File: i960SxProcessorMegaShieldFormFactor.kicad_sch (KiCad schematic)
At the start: 35 parts, among them P1 Power, P2 Data Lines Lower, P3 Data Lines Upper, P4 Address Lines, P5 PWM, P6 Serializable Pins, P7 1284p Direct Connection, U1 74HC245, U2 74HC245, U3 80960Sx

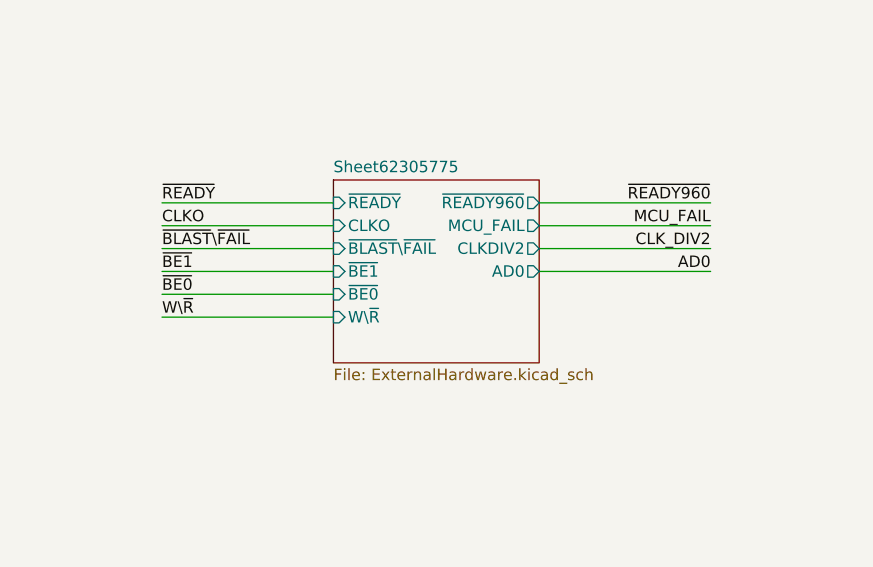
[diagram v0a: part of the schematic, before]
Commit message: Use PLCC20 for the GAL chip instead of the much larger DIP20
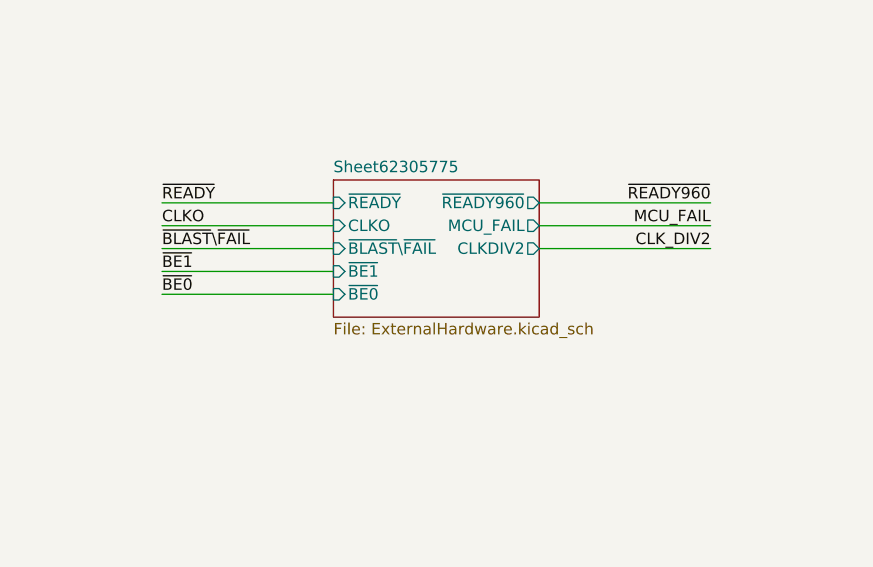
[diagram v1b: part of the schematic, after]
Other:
- sheet Sheet62305775 ports: added none; removed AD0, W\~{R}
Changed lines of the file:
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@@
-    (stroke (width 0) (type default) (color 0 0 0 0))
-  )
-  (wire (pts (xy 323.85 205.74) (xy 342.9 205.74))
     (stroke (width 0) (type default) (color 0 0 0 0))
   )
@@
   )
   (wire (pts (xy 93.98 90.17) (xy 63.5 90.17))
-    (stroke (width 0) (type default) (color 0 0 0 0))
-  )
-  (wire (pts (xy 365.76 200.66) (xy 384.81 200.66))
     (stroke (width 0) (type default) (color 0 0 0 0))
   )
@@
   )
   (label "A18" (at 63.5 77.47 180)
-    (effects (font (size 1.27 1.27)) (justify right bottom))
-  )
-  (label "W\\~{R}" (at 323.85 205.74 0)
-    (effects (font (size 1.27 1.27)) (justify left bottom))
-  )
-  (label "AD0" (at 384.81 200.66 180)
     (effects (font (size 1.27 1.27)) (justify right bottom))
   )
@@
     (pin "1")
   )
-  (sheet (at 342.9 190.5) (size 22.86 20.32) (fields_autoplaced)
+  (sheet (at 342.9 190.5) (size 22.86 15.24) (fields_autoplaced)
     (stroke (width 0) (type solid) (color 0 0 0 0))
     (fill (color 0 0 0 0.0000))
@@
       (effects (font (size 1.27 1.27)) (justify left bottom))
     )
-    (property "Sheet file" "ExternalHardware.kicad_sch" (id 1) (at 342.9 211.4046 0)
+    (property "Sheet file" "ExternalHardware.kicad_sch" (id 1) (at 342.9 206.3246 0)
       (effects (font (size 1.27 1.27)) (justify left top))
     )
@@
     )
     (pin "CLKDIV2" output (at 365.76 198.12 0)
-      (effects (font (size 1.27 1.27)) (justify right))
-    )
-    (pin "W\\~{R}" input (at 342.9 205.74 180)
-      (effects (font (size 1.27 1.27)) (justify left))
-    )
-    (pin "AD0" output (at 365.76 200.66 0)
       (effects (font (size 1.27 1.27)) (justify right))
     )
@@
       (reference "#PWR019") (unit 1) (value "GND") (footprint "")
     )
-    (path "/00000000-0000-0000-0000-000062305776/c87d717f-47b5-4cbc-92c9-1f27489443fc"
-      (reference "#PWR020") (unit 1) (value "+5V") (footprint "")
-    )
-    (path "/00000000-0000-0000-0000-000062305776/99f40a50-ee35-472a-8a7f-9dca1993ec33"
-      (reference "#PWR021") (unit 1) (value "GND") (footprint "")
-    )
     (path "/00000000-0000-0000-0000-000056d758f6"
       (reference "#PWR022") (unit 1) (value "GND") (footprint "")
@@
       (reference "C17") (unit 1) (value "0.1uF") (footprint "Capacitor_SMD:C_0805_2012Metric_Pad1.18x1.45mm_HandSolder")
     )
-    (path "/00000000-0000-0000-0000-000062305776/68b9a284-29e4-4461-9b3a-9f4ef09e2dc9"
-      (reference "C18") (unit 1) (value "0.1uF") (footprint "Capacitor_THT:C_Disc_D5.0mm_W2.5mm_P2.50mm")
-    )
     (path "/00000000-0000-0000-0000-000062305776/37cf12d2-9997-4855-9d67-d21913190832"
       (reference "C19") (unit 1) (value "0.1uF") (footprint "Capacitor_THT:C_Disc_D5.0mm_W2.5mm_P2.50mm")
@@
       (reference "U3") (unit 1) (value "80960Sx") (footprint "Package_LCC:PLCC-84_THT-Socket")
     )
-    (path "/00000000-0000-0000-0000-000062305776/9fb0fc0c-649f-4b6a-8681-4c1c3cff265d"
-      (reference "U6") (unit 1) (value "74AHC74") (footprint "Package_SO:SOIC-14_3.9x8.7mm_P1.27mm")
-    )
-    (path "/00000000-0000-0000-0000-000062305776/05566c90-9ff9-4de8-a5f1-1d8176493d23"
-      (reference "U6") (unit 2) (value "74AHC74") (footprint "Package_SO:SOIC-14_3.9x8.7mm_P1.27mm")
-    )
-    (path "/00000000-0000-0000-0000-000062305776/da30d552-383a-40ee-b502-3261b6b0380f"
-      (reference "U6") (unit 3) (value "74AHC74") (footprint "Package_SO:SOIC-14_3.9x8.7mm_P1.27mm")
-    )
     (path "/00000000-0000-0000-0000-000062305776/67f3f848-2b47-48d4-8ef6-b211a1c5ad8a"
       (reference "U7") (unit 1) (value "74AHC74") (footprint "Package_SO:SOIC-14_3.9x8.7mm_P1.27mm")
@@
     )
     (path "/00000000-0000-0000-0000-000062305776/312ed157-03e4-4f79-8162-ee244f6128f1"
-      (reference "U8") (unit 1) (value "GAL16V8") (footprint "Package_DIP:DIP-20_W7.62mm_Socket")
+      (reference "U8") (unit 1) (value "GAL16V8") (footprint "Package_LCC:PLCC-20_THT-Socket")
     )
     (path "/c11f357c-f8ce-40dd-a2b5-d959d6b2f47e"

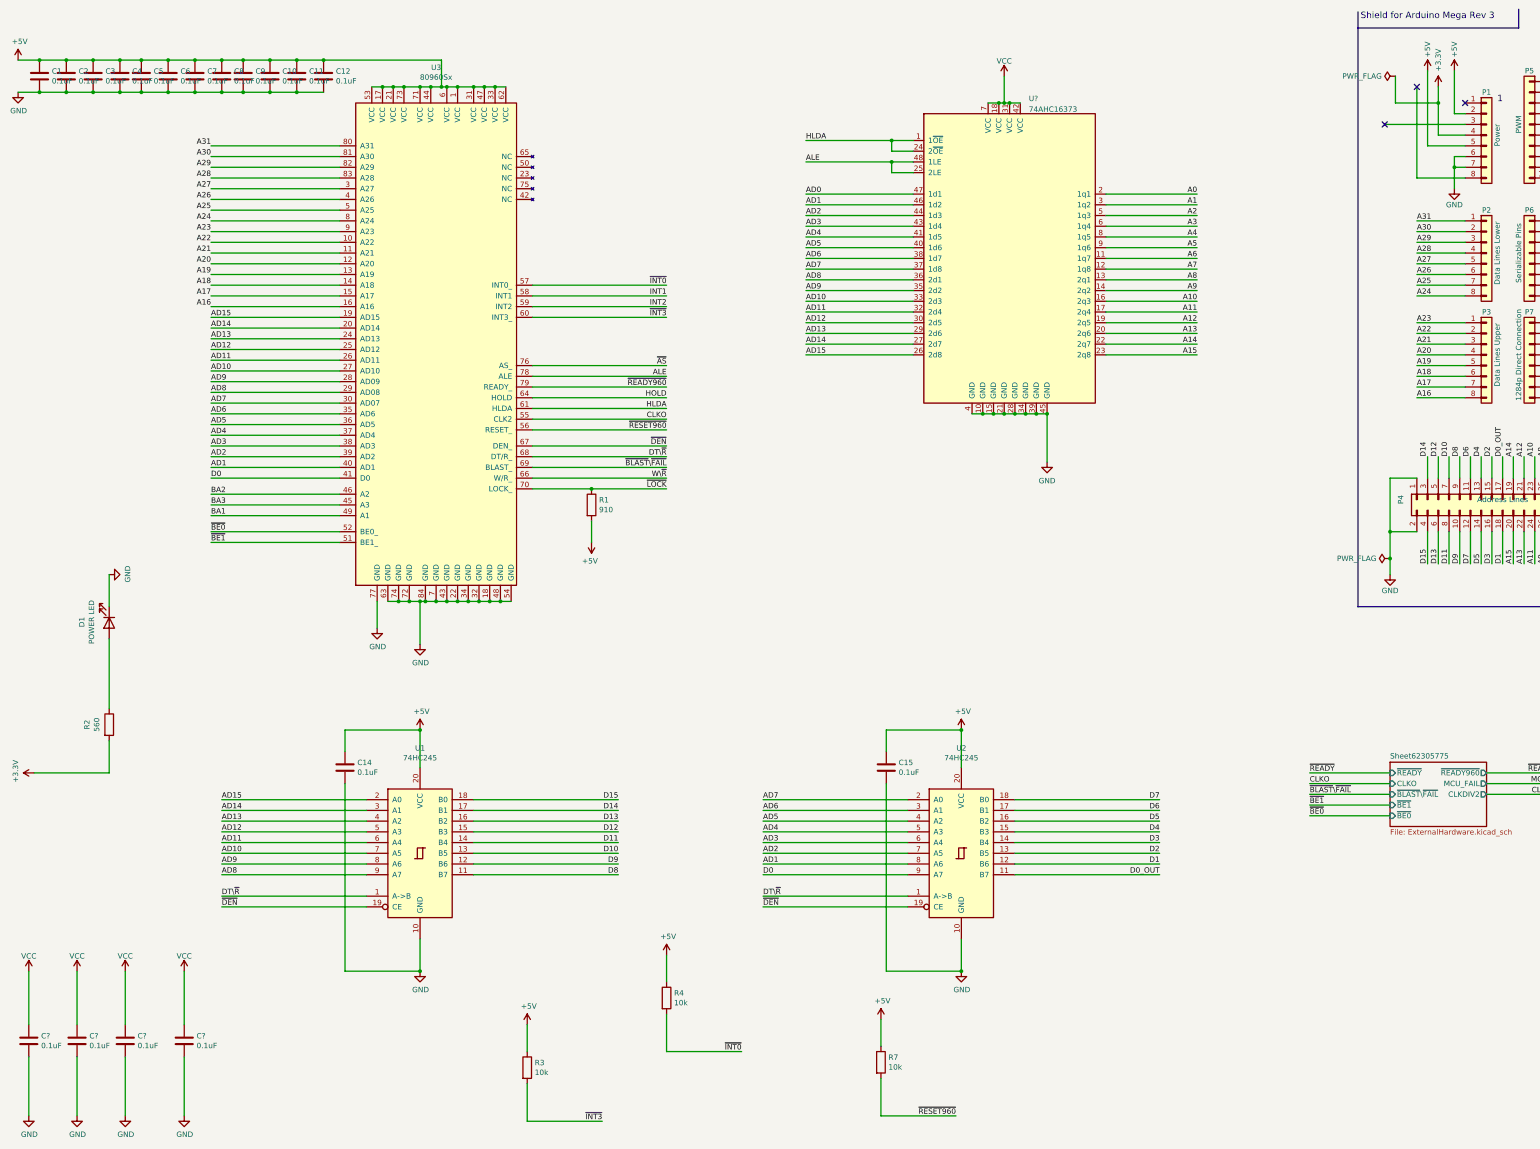
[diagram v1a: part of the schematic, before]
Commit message: Introduce the 74LVC16T245 for the datalines
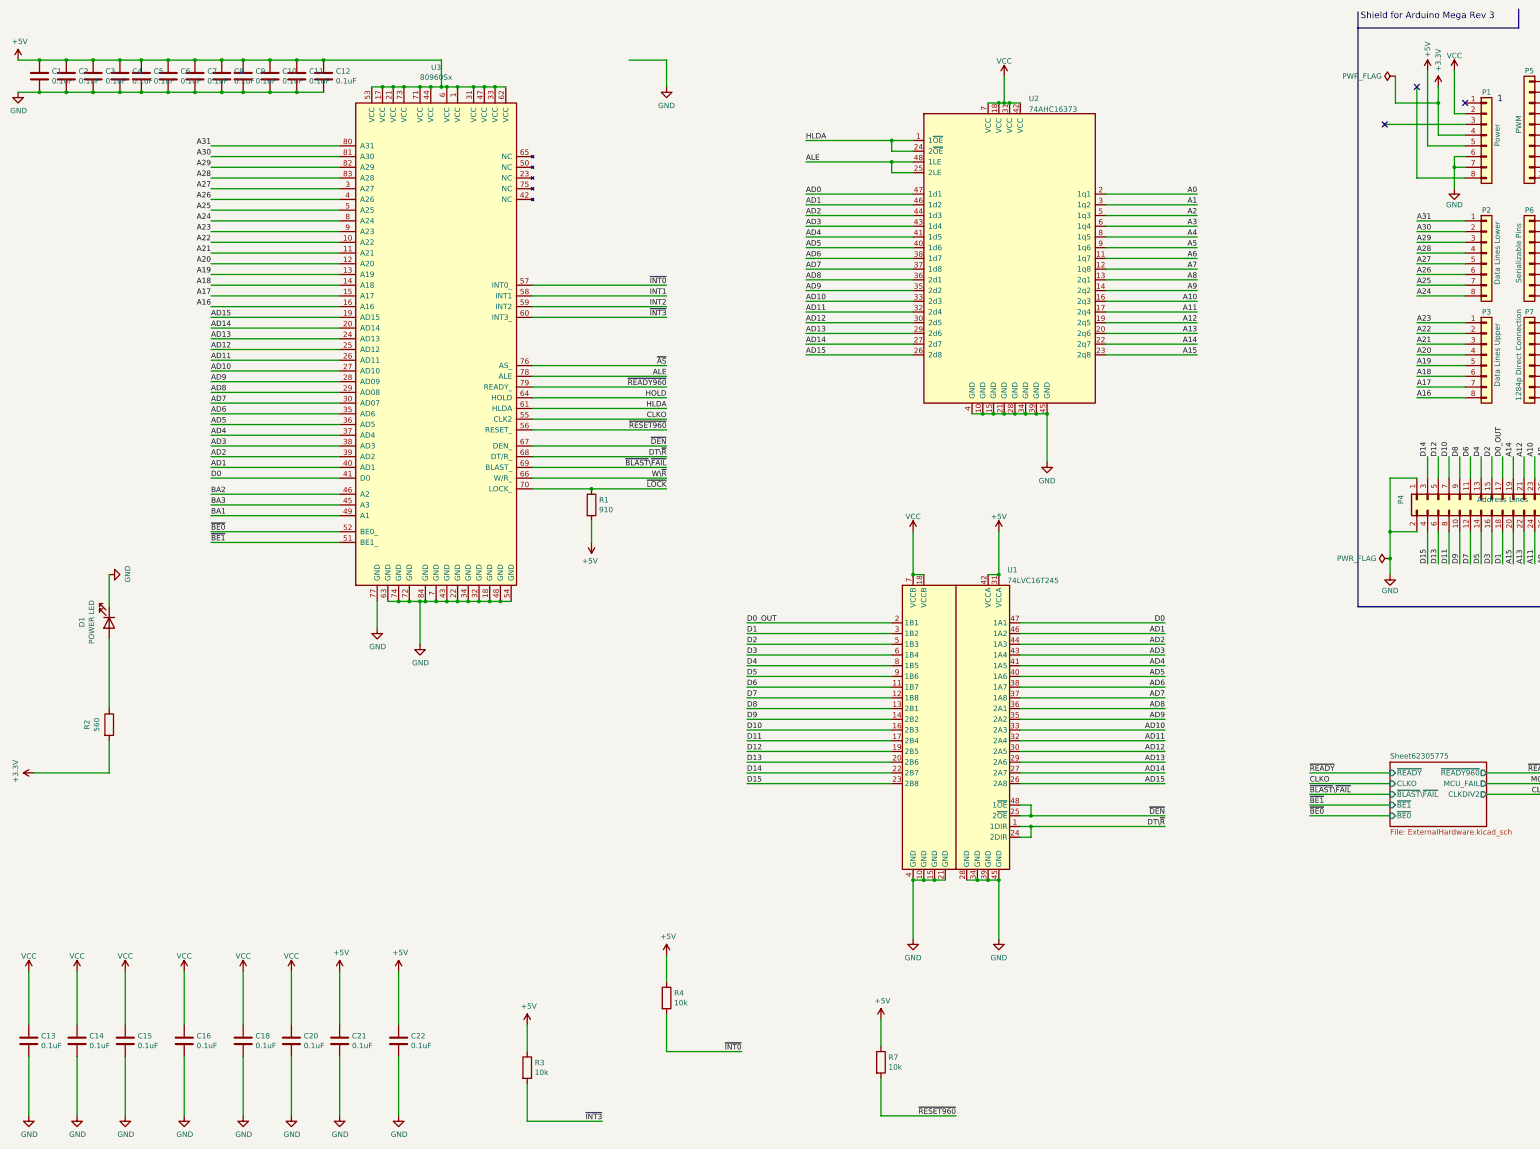
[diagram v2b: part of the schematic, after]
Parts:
- removed C14, C15: 0.1uF, Capacitor_SMD:C_0805_2012Metric_Pad1.18x1.45mm_HandSolder, symbol Device:C
- removed U1, U2: 74HC245, Package_SO:SOIC-20W_7.5x12.8mm_P1.27mm, symbol 74xx:74HC245
- added C18, C20, C21, C22: 0.1uF, Capacitor_SMD:C_0805_2012Metric_Pad1.18x1.45mm_HandSolder, symbol Device:C
- added U1: 74LVC16T245, Package_SO:TSSOP-48_6.1x12.5mm_P0.5mm, symbol LogicLevelTranslators:74LVC16T245
- gave numbers to parts that had none: 5
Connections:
- net +5V: now also C21.1, C22.1, U1.31 (VCCA), U1.42 (VCCA); no longer P1.2 (Pin_2)
- net AD1: now also U1.46 (1A2)
- net AD10: now also U1.33 (2A3)
- net AD11: now also U1.32 (2A4)
- net AD12: now also U1.30 (2A5)
- net AD13: now also U1.29 (2A6)
- net AD14: now also U1.27 (2A7)
- net AD15: now also U1.26 (2A8)
- net AD2: now also U1.44 (1A3)
- net AD3: now also U1.43 (1A4)
- net AD4: now also U1.41 (1A5)
- net AD5: now also U1.40 (1A6)
- net AD6: now also U1.38 (1A7)
- net AD7: now also U1.37 (1A8)
- net AD8: now also U1.36 (2A1)
- net AD9: now also U1.35 (2A2)
- net D0: now also U1.47 (1A1)
- net D0_OUT: now also U1.2 (1B1)
- net D1: now also U1.3 (1B2)
- net D10: now also U1.16 (2B3)
- net D11: now also U1.17 (2B4)
- net D12: now also U1.19 (2B5)
- net D13: now also U1.20 (2B6)
- net D14: now also U1.22 (2B7)
- net D15: now also U1.23 (2B8)
- net D2: now also U1.5 (1B3)
- net D3: now also U1.6 (1B4)
- net D4: now also U1.8 (1B5)
- net D5: now also U1.9 (1B6)
- net D6: now also U1.11 (1B7)
- net D7: now also U1.12 (1B8)
- net D8: now also U1.13 (2B1)
- net D9: now also U1.14 (2B2)
- net DT\~{R}: now also U1.1 (1DIR), U1.24 (2DIR)
- net GND: now also C18.2, C20.2, C21.2, C22.2, U1.10 (GND), U1.15 (GND), U1.21 (GND), U1.28 (GND), U1.34 (GND), U1.39 (GND), U1.4 (GND), U1.45 (GND)
- net VCC: now also P1.2 (Pin_2), C18.1, C20.1, U1.18 (VCCB), U1.7 (VCCB)
- net ~{DEN}: now also U1.25 (2~{OE}), U1.48 (1~{OE})

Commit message: Just do the consolidation
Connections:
- net A0: now also U2.23 (2q8); no longer U2.2 (1q1)
- net A1: now also U2.22 (2q7); no longer U2.3 (1q2)
- net A10: now also U2.9 (1q6); no longer U2.16 (2q3)
- net A11: now also U2.8 (1q5); no longer U2.17 (2q4)
- net A12: now also U2.6 (1q4); no longer U2.19 (2q5)
- net A13: now also U2.5 (1q3); no longer U2.20 (2q6)
- net A14: now also U2.3 (1q2); no longer U2.22 (2q7)
- net A15: now also U2.2 (1q1); no longer U2.23 (2q8)
- net A2: now also U2.20 (2q6); no longer U2.5 (1q3)
- net A3: now also U2.19 (2q5); no longer U2.6 (1q4)
- net A4: now also U2.17 (2q4); no longer U2.8 (1q5)
- net A5: now also U2.16 (2q3); no longer U2.9 (1q6)
- net A6: now also U2.14 (2q2); no longer U2.11 (1q7)
- net A7: now also U2.13 (2q1); no longer U2.12 (1q8)
- net A8: now also U2.12 (1q8); no longer U2.13 (2q1)
- net A9: now also U2.11 (1q7); no longer U2.14 (2q2)
- net AD0: now also U2.26 (2d8); no longer U2.47 (1d1)
- net AD1: now also U1.27 (2A7), U2.27 (2d7); no longer U1.46 (1A2), U2.46 (1d2)
- net AD10: now also U1.40 (1A6), U2.40 (1d6); no longer U1.33 (2A3), U2.33 (2d3)
- net AD11: now also U1.41 (1A5), U2.41 (1d5); no longer U1.32 (2A4), U2.32 (2d4)
- net AD12: now also U1.43 (1A4), U2.43 (1d4); no longer U1.30 (2A5), U2.30 (2d5)
- net AD13: now also U1.44 (1A3), U2.44 (1d3); no longer U1.29 (2A6), U2.29 (2d6)
- net AD14: now also U1.46 (1A2), U2.46 (1d2); no longer U1.27 (2A7), U2.27 (2d7)
- net AD15: now also U1.47 (1A1), U2.47 (1d1); no longer U1.26 (2A8), U2.26 (2d8)
- net AD2: now also U1.29 (2A6), U2.29 (2d6); no longer U1.44 (1A3), U2.44 (1d3)
- net AD3: now also U1.30 (2A5), U2.30 (2d5); no longer U1.43 (1A4), U2.43 (1d4)
- net AD4: now also U1.32 (2A4), U2.32 (2d4); no longer U1.41 (1A5), U2.41 (1d5)
- net AD5: now also U1.33 (2A3), U2.33 (2d3); no longer U1.40 (1A6), U2.40 (1d6)
- net AD6: now also U1.35 (2A2), U2.35 (2d2); no longer U1.38 (1A7), U2.38 (1d7)
- net AD7: now also U1.36 (2A1), U2.36 (2d1); no longer U1.37 (1A8), U2.37 (1d8)
- net AD8: now also U1.37 (1A8), U2.37 (1d8); no longer U1.36 (2A1), U2.36 (2d1)
- net AD9: now also U1.38 (1A7), U2.38 (1d7); no longer U1.35 (2A2), U2.35 (2d2)
- net D0: now also U1.26 (2A8); no longer U1.47 (1A1)
- net D0_OUT: now also U1.23 (2B8); no longer U1.2 (1B1)
- net D1: now also U1.22 (2B7); no longer U1.3 (1B2)
- net D10: now also U1.9 (1B6); no longer U1.16 (2B3)
- net D11: now also U1.8 (1B5); no longer U1.17 (2B4)
- net D12: now also U1.6 (1B4); no longer U1.19 (2B5)
- net D13: now also U1.5 (1B3); no longer U1.20 (2B6)
- net D14: now also U1.3 (1B2); no longer U1.22 (2B7)
- net D15: now also U1.2 (1B1); no longer U1.23 (2B8)
- net D2: now also U1.20 (2B6); no longer U1.5 (1B3)
- net D3: now also U1.19 (2B5); no longer U1.6 (1B4)
- net D4: now also U1.17 (2B4); no longer U1.8 (1B5)
- net D5: now also U1.16 (2B3); no longer U1.9 (1B6)
- net D6: now also U1.14 (2B2); no longer U1.11 (1B7)
- net D7: now also U1.13 (2B1); no longer U1.12 (1B8)
- net D8: now also U1.12 (1B8); no longer U1.13 (2B1)
- net D9: now also U1.11 (1B7); no longer U1.14 (2B2)

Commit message: Finished retracing
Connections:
- net AD0 is gone; now on net GND: U2.26 (2d8)
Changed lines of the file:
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@@
+    (effects (font (size 1.27 1.27)) (justify left bottom))
+  )
+  (label "AD0" (at 162.56 24.13 0)
     (effects (font (size 1.27 1.27)) (justify left bottom))
   )

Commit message: Remove a resistor and drop the 10MHz output clock
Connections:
- net CLK_DIV2: no longer P5.1 (Pin_1)
- net ~{READY}: no longer P5.6 (Pin_6)
- no-connect marks 4 -> 6
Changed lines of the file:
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@@
   (no_connect (at 349.25 30.48))
   (no_connect (at 398.78 39.37))
+  (no_connect (at 398.78 41.91))
   (no_connect (at 341.63 39.37))
   (no_connect (at 360.68 34.29))
+  (no_connect (at 398.78 29.21))
   (wire (pts (xy 381 46.99) (xy 398.78 46.99))
     (stroke (width 0) (type default) (color 0 0 0 0))
@@
     (effects (font (size 1.27 1.27)) (justify left bottom))
   )
-  (label "~{READY}" (at 398.78 41.91 180)
-    (effects (font (size 1.27 1.27)) (justify right bottom))
-  )
   (label "~{INT3}" (at 156.21 275.59 180)
     (effects (font (size 1.27 1.27)) (justify right bottom))
@@
     (effects (font (size 1.27 1.27)) (justify right bottom))
   )
-  (label "CLK_DIV2" (at 398.78 29.21 180)
-    (effects (font (size 1.27 1.27)) (justify right bottom))
-  )
   (label "AD9" (at 63.5 100.33 0)
     (effects (font (size 1.27 1.27)) (justify left bottom))
@@
       (reference "#PWR026") (unit 1) (value "GND") (footprint "")
     )
-    (path "/00000000-0000-0000-0000-000062305776/7e6268bd-de28-4e45-b872-c2d5289de35e"
-      (reference "#PWR027") (unit 1) (value "+5V") (footprint "")
-    )
     (path "/00000000-0000-0000-0000-000062305776/0e2482b9-a689-45a3-a536-674e09a602a2"
       (reference "#PWR028") (unit 1) (value "+5V") (footprint "")
@@
       (reference "R4") (unit 1) (value "10k") (footprint "Resistor_SMD:R_0805_2012Metric_Pad1.20x1.40mm_HandSolder")
     )
-    (path "/00000000-0000-0000-0000-000062305776/c5053a4e-ffe0-455f-8838-52320f5821ec"
-      (reference "R5") (unit 1) (value "10k") (footprint "Resistor_SMD:R_0805_2012Metric_Pad1.20x1.40mm_HandSolder")
-    )
     (path "/00000000-0000-0000-0000-000062305776/ba417558-e07a-4aa8-8f8c-15d6dc468305"

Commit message: Broke the link
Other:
- sheet Sheet62305775 ports: added none; removed CLKDIV2
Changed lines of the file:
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@@
-    (stroke (width 0) (type default) (color 0 0 0 0))
-  )
-  (wire (pts (xy 365.76 198.12) (xy 384.81 198.12))
     (stroke (width 0) (type default) (color 0 0 0 0))
   )
@@
   (label "D6" (at 190.5 180.34 0)
     (effects (font (size 1.27 1.27)) (justify left bottom))
-  )
-  (label "CLK_DIV2" (at 384.81 198.12 180)
-    (effects (font (size 1.27 1.27)) (justify right bottom))
   )
   (label "AD5" (at 204.47 81.28 0)
@@
       (effects (font (size 1.27 1.27)) (justify left))
     )
-    (pin "CLKDIV2" output (at 365.76 198.12 0)
-      (effects (font (size 1.27 1.27)) (justify right))
-    )
-  )
+  )
